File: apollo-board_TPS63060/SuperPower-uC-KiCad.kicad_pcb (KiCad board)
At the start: 4 copper layers, 45.1 x 45.1 mm, 113 parts, among them J1 JST_PH_S2B_thru, J10 Conn_01x13_Male, J11 Conn_01x04_Male, J3 Conn_01x02_Male, J4 DNP/JST_ZH_S2B_thru, J5 DNP/JST_XH_S2B_thru, J6 Conn_01x02_Male, Q1 DMN2019UTS, Q10 2N7002A, Q11 2N7002A, Q12 DMP2035UVT, Q13 DMP2035UVT, Q14 DMP2035UVT, Q15 DMN3023L, Q2 Si3421DV, Q3 DMN3023L, Q4 2N7002A, Q5 DMP2035UVT, Q6 BSS84-7-F, Q9 2N7002A, SW1 DNP/SKRKAEE020, U1 AP9101CK6-AYTRG1, U10 TPS63060, U2 USB-C, U3 IP4220CZ6, U4 LTC4162EUFD-LAD, U5 RV-3028-C7, U6 TPS70933DBV, U9 TPS63060

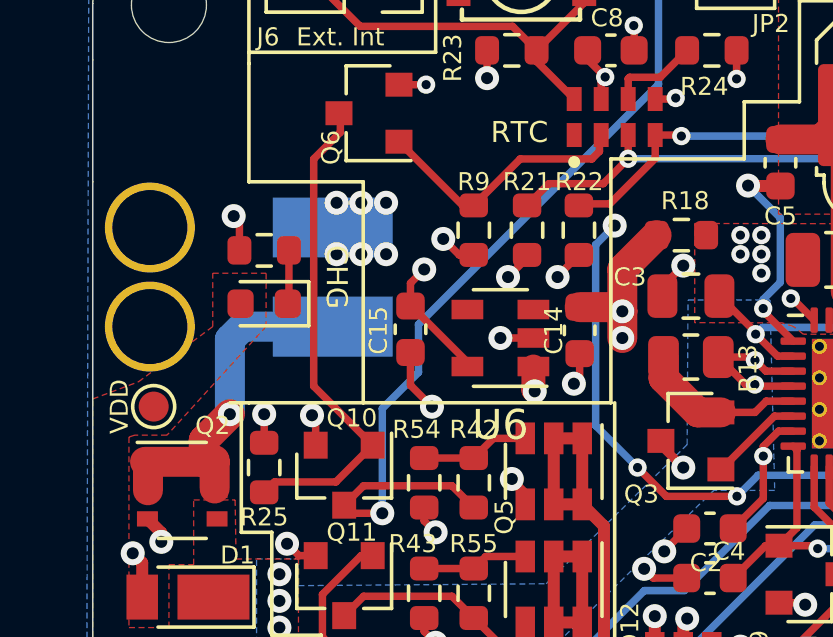
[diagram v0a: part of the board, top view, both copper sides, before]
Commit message: Update and clean "charger" sheet + add "Vcc" test point
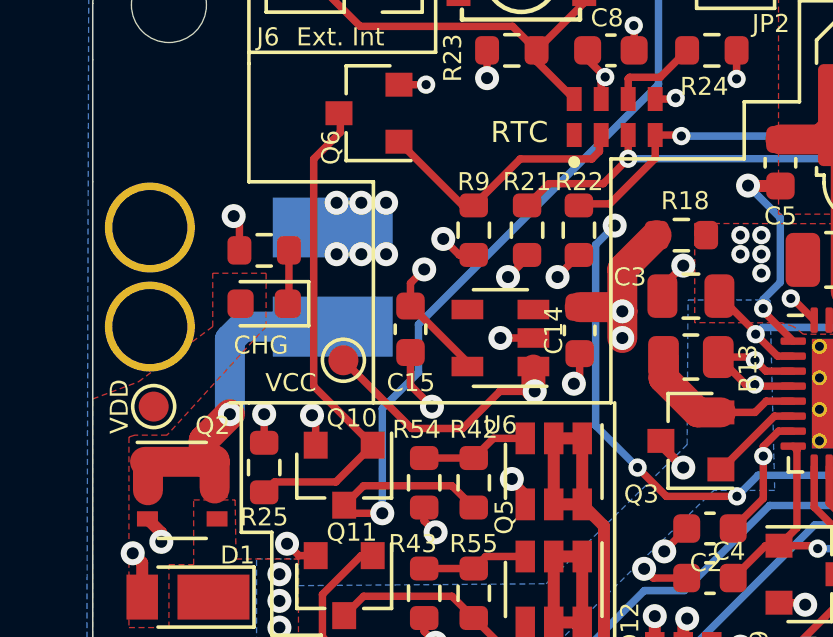
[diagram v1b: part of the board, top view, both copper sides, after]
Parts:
- added TP6: 3V3_I2C, TestPoint:TestPoint_Pad_D1.0mm, F.Cu at (126.3, 89.5)
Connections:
- C14 pad 1: /RTC/VIN -> VCC
- C7 pad 1: VCC -> VCCQ
- Q12 pad 1: /RTC/VIN -> VCC
- Q12 pad 2: /RTC/VIN -> VCC
- Q12 pad 4: VCC -> VCCQ
- Q12 pad 5: /RTC/VIN -> VCC
- Q12 pad 6: /RTC/VIN -> VCC
- Q14 pad 4: /RTC/VIN -> VCC
- Q15 pad 3: VCC -> VCCQ
- Q5 pad 4: /RTC/VIN -> VCC
- R13 pad 1: VCC -> VCCQ
- R17 pad 1: VCC -> VCCQ
- R18 pad 1: /RTC/VIN -> VCC
- R18 pad 2: VCC -> VCCQ
- R42 pad 2: /RTC/VIN -> VCC
- R43 pad 2: /RTC/VIN -> VCC
- U4 pad 27: VCC -> VCCQ
- U4 pad 28: VCC -> VCCQ
- U4 pad 3: VCC -> VCCQ
- U4 pad 4: VCC -> VCCQ
- U6 pad 1: /RTC/VIN -> VCC
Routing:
- net /RTC/VIN: track 14.6 -> 0.00 mm, vias 11 -> 0
- net VCC: track 10.1 -> 22.4 mm
- net VCCQ: track 0.00 -> 10.1 mm, vias 0 -> 11
- added copper zone on F.Cu, net VCCQ
- added copper zone on In2.Cu, net VCCQ
- removed copper zone on In2.Cu, net /RTC/VIN
- removed copper zone on F.Cu, net VCC
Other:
- board text added: "VCC"

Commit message: Rename some power signal on Schematic to improve readability.
+ Misc. updates
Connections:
- net /~SMBALERT renamed Net-(J10-Pad13)

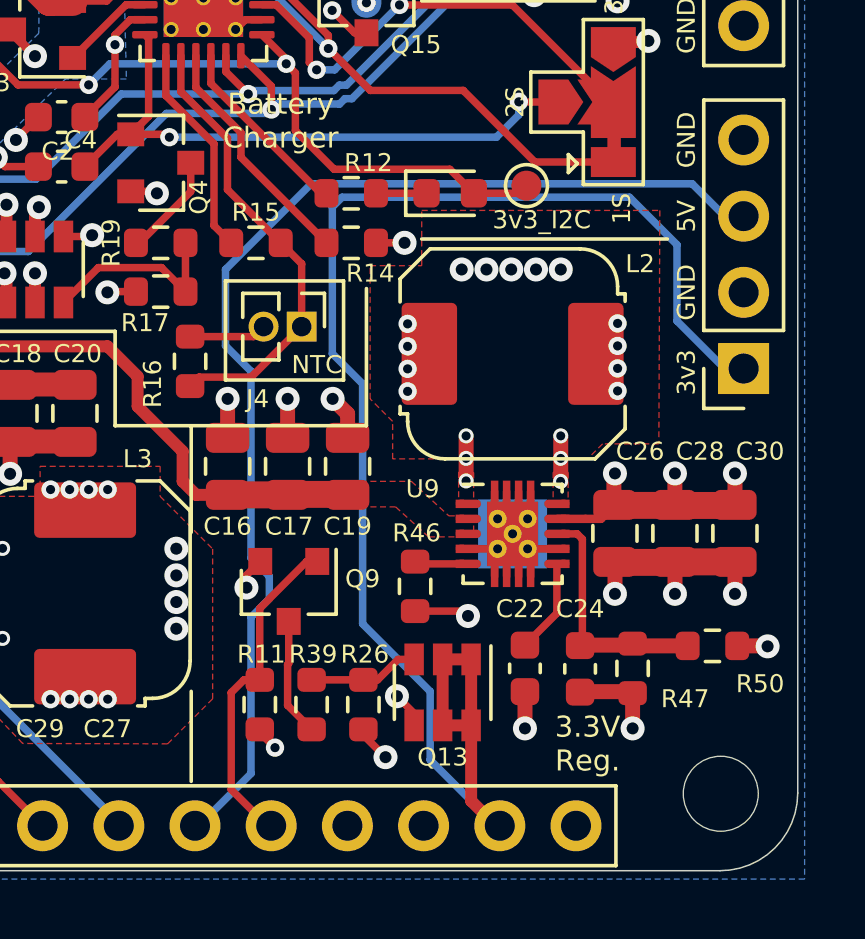
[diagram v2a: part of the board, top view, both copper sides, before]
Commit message: Improve Power tracks width on Bottom Layer
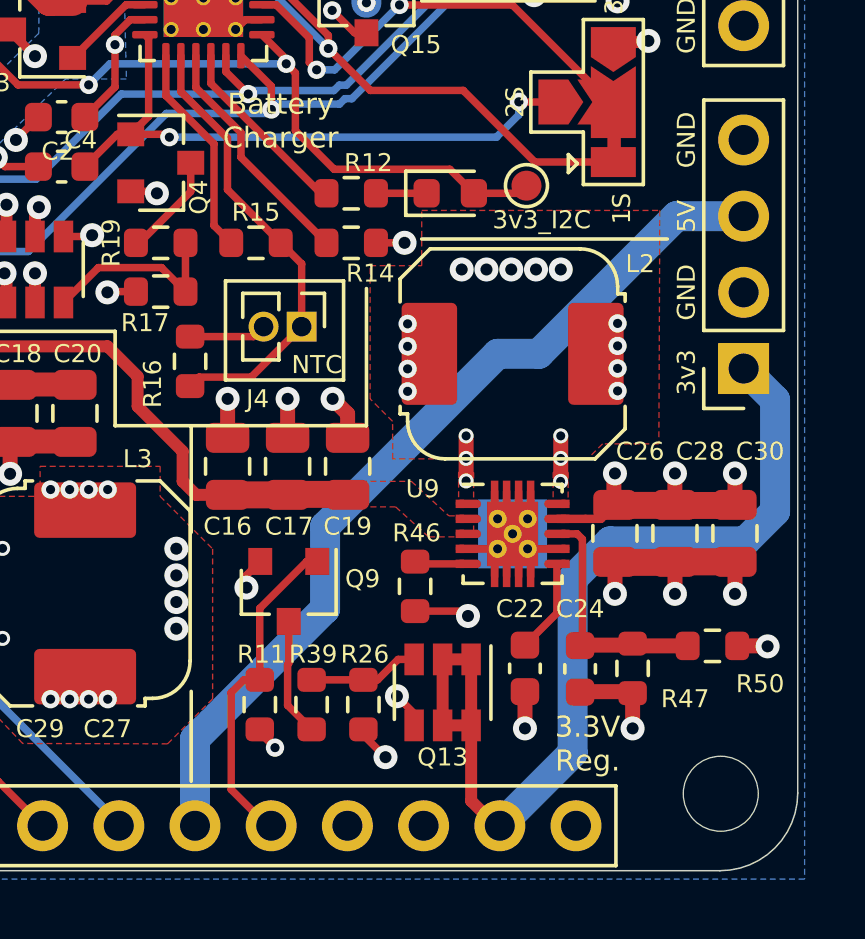
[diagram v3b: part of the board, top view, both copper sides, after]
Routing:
- net /3v3: track 50.3 -> 32.3 mm
- net /5V: track 61.7 -> 53.1 mm
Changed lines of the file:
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@@
     (thickness 1.6)
     (drawings 122)
-    (tracks 1000)
+    (tracks 992)
     (zones 0)
     (modules 114)
@@
     (1 In1.Cu power hide)
     (2 In2.Cu signal hide)
-    (31 B.Cu signal hide)
+    (31 B.Cu signal)
     (32 B.Adhes user)
     (33 F.Adhes user)
@@
   )
   (setup
-    (last_trace_width 0.25)
+    (last_trace_width 1)
     (user_trace_width 0.2)
     (user_trace_width 0.25)
@@
   (via (at 128.589 113.515) (size 0.8) (drill 0.4) (layers F.Cu B.Cu) (net 59))
   (via (at 130.589 114.265) (size 0.8) (drill 0.4) (layers F.Cu B.Cu) (net 59))
-  (segment (start 159.574989 97.344989) (end 160.655 98.425) (width 0.25) (layer B.Cu) (net 59))
-  (segment (start 146.876011 97.344989) (end 159.574989 97.344989) (width 0.25) (layer B.Cu) (net 59))
-  (segment (start 144.018 102.743) (end 144.018 100.203) (width 0.25) (layer B.Cu) (net 59))
-  (segment (start 144.870001 109.824499) (end 144.870001 103.595001) (width 0.25) (layer B.Cu) (net 59))
-  (segment (start 145.4785 111.182002) (end 145.4785 110.432998) (width 0.25) (layer B.Cu) (net 59))
-  (segment (start 144.870001 103.595001) (end 144.018 102.743) (width 0.25) (layer B.Cu) (net 59))
-  (segment (start 145.4785 110.432998) (end 144.870001 109.824499) (width 0.25) (layer B.Cu) (net 59))
-  (segment (start 144.870001 111.790501) (end 145.4785 111.182002) (width 0.25) (layer B.Cu) (net 59))
-  (segment (start 144.018 100.203) (end 146.876011 97.344989) (width 0.25) (layer B.Cu) (net 59))
-  (segment (start 144.870001 117.003999) (end 144.870001 111.790501) (width 0.25) (layer B.Cu) (net 59))
-  (segment (start 143.002 118.872) (end 144.870001 117.003999) (width 0.25) (layer B.Cu) (net 59))
   (segment (start 129.5 114.3) (end 131.5 114.3) (width 0.8) (layer F.Cu) (net 59))
   (segment (start 133.5 114.3) (end 131.5 114.3) (width 0.8) (layer F.Cu) (net 59))
@@
   (segment (start 133.839 113.961) (end 133.5 114.3) (width 0.25) (layer F.Cu) (net 59))
   (segment (start 133.839 112.475) (end 133.839 113.961) (width 0.28) (layer F.Cu) (net 59))
+  (segment (start 159.052799 98.425) (end 161.29 98.425) (width 1) (layer B.Cu) (net 59))
+  (segment (start 154.462799 103.015) (end 159.052799 98.425) (width 1) (layer B.Cu) (net 59))
+  (segment (start 153.089 103.015) (end 154.462799 103.015) (width 1) (layer B.Cu) (net 59))
+  (segment (start 147.339 108.765) (end 153.089 103.015) (width 1) (layer B.Cu) (net 59))
+  (segment (start 147.339 111.515) (end 147.339 108.765) (width 1) (layer B.Cu) (net 59))
+  (segment (start 143.002 115.852) (end 147.339 111.515) (width 1) (layer B.Cu) (net 59))
+  (segment (start 143.002 118.745) (end 143.002 115.852) (width 1) (layer B.Cu) (net 59))
   (segment (start 152.207 113.2) (end 151.257 113.2) (width 0.4) (layer F.Cu) (net 60))
   (segment (start 151.257 113.2) (end 151.257 115.4) (width 0.4) (layer F.Cu) (net 60))
@@
   (segment (start 152.207 117.917) (end 153.162 118.872) (width 0.4) (layer F.Cu) (net 60))
   (segment (start 152.207 115.4) (end 152.207 117.917) (width 0.4) (layer F.Cu) (net 60))
-  (segment (start 147.906599 97.794999) (end 157.484999 97.794999) (width 0.25) (layer B.Cu) (net 60))
-  (segment (start 157.484999 97.794999) (end 159.0675 99.3775) (width 0.25) (layer B.Cu) (net 60))
-  (segment (start 147.578999 98.122599) (end 147.906599 97.794999) (width 0.25) (layer B.Cu) (net 60))
-  (segment (start 147.578999 103.004999) (end 147.578999 98.122599) (width 0.25) (layer B.Cu) (net 60))
-  (segment (start 148.589 104.015) (end 147.578999 103.004999) (width 0.25) (layer B.Cu) (net 60))
-  (segment (start 148.589 112.015) (end 148.589 104.015) (width 0.25) (layer B.Cu) (net 60))
-  (segment (start 150.839 114.265) (end 148.589 112.015) (width 0.25) (layer B.Cu) (net 60))
-  (segment (start 159.0675 101.9175) (end 160.655 103.505) (width 0.25) (layer B.Cu) (net 60))
-  (segment (start 150.839 116.549) (end 150.839 114.265) (width 0.25) (layer B.Cu) (net 60))
-  (segment (start 159.0675 99.3775) (end 159.0675 101.9175) (width 0.25) (layer B.Cu) (net 60))
-  (segment (start 153.162 118.872) (end 150.839 116.549) (width 0.25) (layer B.Cu) (net 60))
+  (segment (start 162.339 104.554) (end 161.29 103.505) (width 1) (layer B.Cu) (net 60))
+  (segment (start 161.339 109.265) (end 162.339 108.265) (width 1) (layer B.Cu) (net 60))
+  (segment (start 156.839 109.265) (end 161.339 109.265) (width 1) (layer B.Cu) (net 60))
+  (segment (start 162.339 108.265) (end 162.339 104.554) (width 1) (layer B.Cu) (net 60))
+  (segment (start 155.589 110.515) (end 156.839 109.265) (width 1) (layer B.Cu) (net 60))
+  (segment (start 155.589 116.318) (end 155.589 110.515) (width 1) (layer B.Cu) (net 60))
+  (segment (start 153.162 118.745) (end 155.589 116.318) (width 1) (layer B.Cu) (net 60))
   (via (at 162.089 112.765) (size 0.8) (drill 0.4) (layers F.Cu B.Cu) (net 61))
   (via (at 149.352 116.459) (size 0.8) (drill 0.4) (layers F.Cu B.Cu) (net 61))

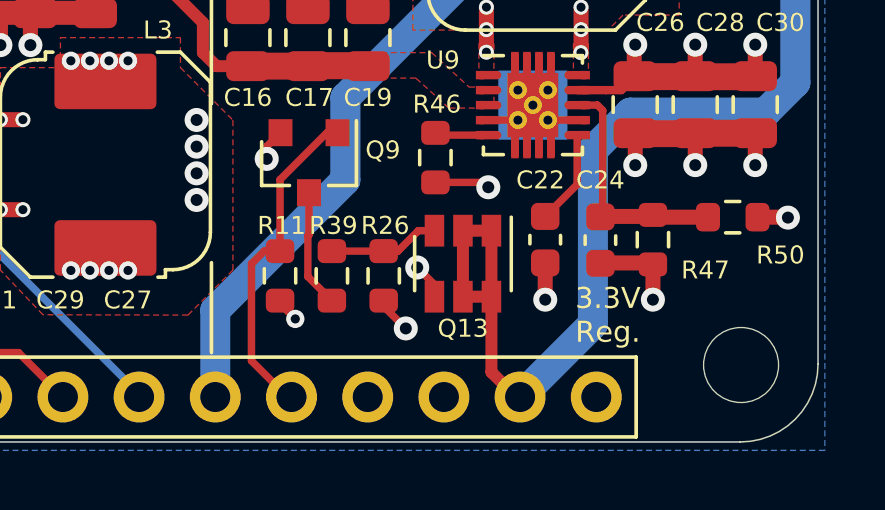
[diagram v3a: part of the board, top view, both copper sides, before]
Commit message: Improve Power Tracks width and Vias on Top Layer (+3.3V regulator)
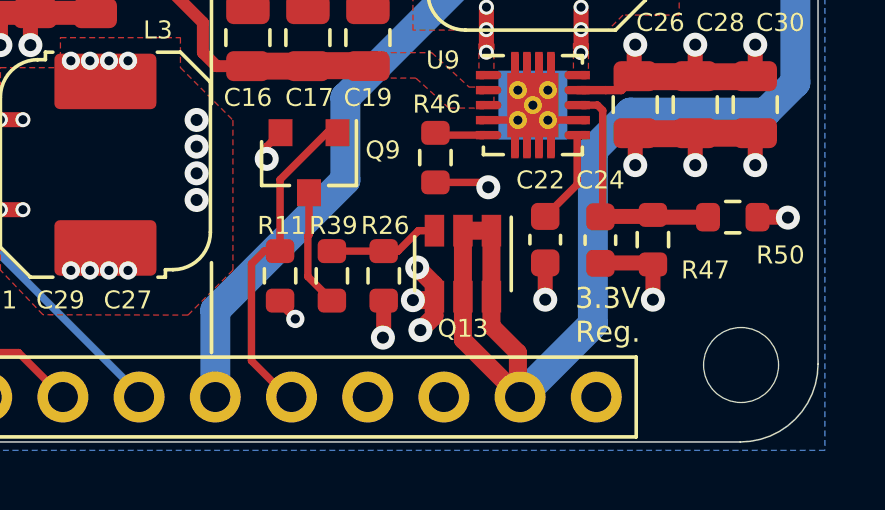
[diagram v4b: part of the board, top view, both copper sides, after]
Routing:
- net /3v3: track 32.3 -> 35.5 mm
- net /3v3_MCU: track 14.5 -> 16.6 mm, vias 7 -> 9
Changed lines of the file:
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@@
     (thickness 1.6)
     (drawings 122)
-    (tracks 992)
+    (tracks 1001)
     (zones 0)
     (modules 114)
@@
     (0 F.Cu signal)
     (1 In1.Cu power hide)
-    (2 In2.Cu signal hide)
-    (31 B.Cu signal)
+    (2 In2.Cu signal)
+    (31 B.Cu signal hide)
     (32 B.Adhes user)
     (33 F.Adhes user)
@@
   )
   (setup
-    (last_trace_width 1)
+    (last_trace_width 0.5)
     (user_trace_width 0.2)
     (user_trace_width 0.25)
@@
     (user_trace_width 0.4)
     (user_trace_width 0.5)
+    (user_trace_width 0.6)
     (user_trace_width 0.8)
     (user_trace_width 1)
@@
   (segment (start 143.002 115.852) (end 147.339 111.515) (width 1) (layer B.Cu) (net 59))
   (segment (start 143.002 118.745) (end 143.002 115.852) (width 1) (layer B.Cu) (net 59))
-  (segment (start 152.207 113.2) (end 151.257 113.2) (width 0.4) (layer F.Cu) (net 60))
-  (segment (start 151.257 113.2) (end 151.257 115.4) (width 0.4) (layer F.Cu) (net 60))
-  (segment (start 151.257 115.4) (end 152.207 115.4) (width 0.4) (layer F.Cu) (net 60))
-  (segment (start 152.207 113.2) (end 152.207 115.4) (width 0.4) (layer F.Cu) (net 60))
-  (segment (start 152.207 117.917) (end 153.162 118.872) (width 0.4) (layer F.Cu) (net 60))
-  (segment (start 152.207 115.4) (end 152.207 117.917) (width 0.4) (layer F.Cu) (net 60))
+  (segment (start 152.207 113.2) (end 151.257 113.2) (width 0.6) (layer F.Cu) (net 60))
+  (segment (start 151.257 113.2) (end 151.257 115.4) (width 0.6) (layer F.Cu) (net 60))
+  (segment (start 152.207 113.2) (end 152.207 115.4) (width 0.6) (layer F.Cu) (net 60))
   (segment (start 162.339 104.554) (end 161.29 103.505) (width 1) (layer B.Cu) (net 60))
   (segment (start 161.339 109.265) (end 162.339 108.265) (width 1) (layer B.Cu) (net 60))
@@
   (segment (start 155.589 116.318) (end 155.589 110.515) (width 1) (layer B.Cu) (net 60))
   (segment (start 153.162 118.745) (end 155.589 116.318) (width 1) (layer B.Cu) (net 60))
+  (segment (start 153.089 118.799) (end 153.162 118.872) (width 0.5) (layer F.Cu) (net 60))
+  (segment (start 153.089 117.265) (end 153.089 118.799) (width 0.6) (layer F.Cu) (net 60))
+  (segment (start 152.207 116.383) (end 153.089 117.265) (width 0.6) (layer F.Cu) (net 60))
+  (segment (start 152.207 115.4) (end 152.207 116.383) (width 0.6) (layer F.Cu) (net 60))
+  (segment (start 151.257 116.84) (end 153.162 118.745) (width 0.6) (layer F.Cu) (net 60))
+  (segment (start 151.257 115.4) (end 151.257 116.84) (width 0.6) (layer F.Cu) (net 60))
   (via (at 162.089 112.765) (size 0.8) (drill 0.4) (layers F.Cu B.Cu) (net 61))
-  (via (at 149.352 116.459) (size 0.8) (drill 0.4) (layers F.Cu B.Cu) (net 61))
-  (segment (start 148.6154 115.7224) (end 149.352 116.459) (width 0.25) (layer F.Cu) (net 61))
-  (segment (start 148.6154 115.5314) (end 148.6154 115.7224) (width 0.25) (layer F.Cu) (net 61))
   (via (at 149.733 114.427) (size 0.8) (drill 0.4) (layers F.Cu B.Cu) (net 61))
-  (segment (start 150.307 115.001) (end 149.733 114.427) (width 0.25) (layer F.Cu) (net 61))
-  (segment (start 150.307 115.4) (end 150.307 115.001) (width 0.25) (layer F.Cu) (net 61))
+  (segment (start 150.307 115.4) (end 150.307 115.001) (width 0.6) (layer F.Cu) (net 61))
+  (segment (start 150.307 115.001) (end 149.733 114.427) (width 0.6) (layer F.Cu) (net 61))
   (via (at 157 107) (size 0.8) (drill 0.4) (layers F.Cu B.Cu) (net 61))
   (segment (start 156.9658 108.0664) (end 156.9658 107.1103) (width 0.5) (layer F.Cu) (net 61))
@@
   (segment (start 151.914 111.59) (end 152.076347 111.752347) (width 0.25) (layer F.Cu) (net 61))
   (segment (start 150.339 111.59) (end 151.914 111.59) (width 0.25) (layer F.Cu) (net 61))
+  (via (at 149.589 115.515) (size 0.8) (drill 0.4) (layers F.Cu B.Cu) (net 61))
+  (via (at 149.839007 116.514993) (size 0.8) (drill 0.4) (layers F.Cu B.Cu) (net 61))
+  (segment (start 150.307 115.4) (end 150.307 116.047) (width 0.6) (layer F.Cu) (net 61))
+  (segment (start 150.307 116.047) (end 149.839007 116.514993) (width 0.6) (layer F.Cu) (net 61))
+  (segment (start 150.192 115.515) (end 150.307 115.4) (width 0.5) (layer F.Cu) (net 61))
+  (segment (start 149.589 115.515) (end 150.192 115.515) (width 0.6) (layer F.Cu) (net 61))
+  (segment (start 148.6154 116.7386) (end 148.589 116.765) (width 0.5) (layer F.Cu) (net 61))
+  (segment (start 148.6154 115.5314) (end 148.6154 116.7386) (width 0.5) (layer F.Cu) (net 61))
+  (via (at 148.589 116.765) (size 0.8) (drill 0.4) (layers F.Cu B.Cu) (net 61))
   (segment (start 138.93289 93.152) (end 138.922 93.152) (width 0.25) (layer F.Cu) (net 62))
   (segment (start 140.70769 91.3772) (end 138.93289 93.152) (width 0.25) (layer F.Cu) (net 62))
@@
     (polygon
       (pts
-        (xy 162.306 116.713) (xy 149.86 116.713) (xy 149.86 120.269) (xy 146.431 120.269) (xy 146.431 110.2995)
-        (xy 149.5425 110.2995) (xy 156.339 110.28225) (xy 156.339 107.015) (xy 157.089 106.265) (xy 162.306 106.265)
+        (xy 162.306 116.713) (xy 150.839 116.765) (xy 149.86 117.515) (xy 149.86 120.269) (xy 146.431 120.269)
+        (xy 146.431 110.2995) (xy 149.5425 110.2995) (xy 156.339 110.28225) (xy 156.339 107.015) (xy 157.089 106.265)
+        (xy 162.306 106.265)
       )
     )

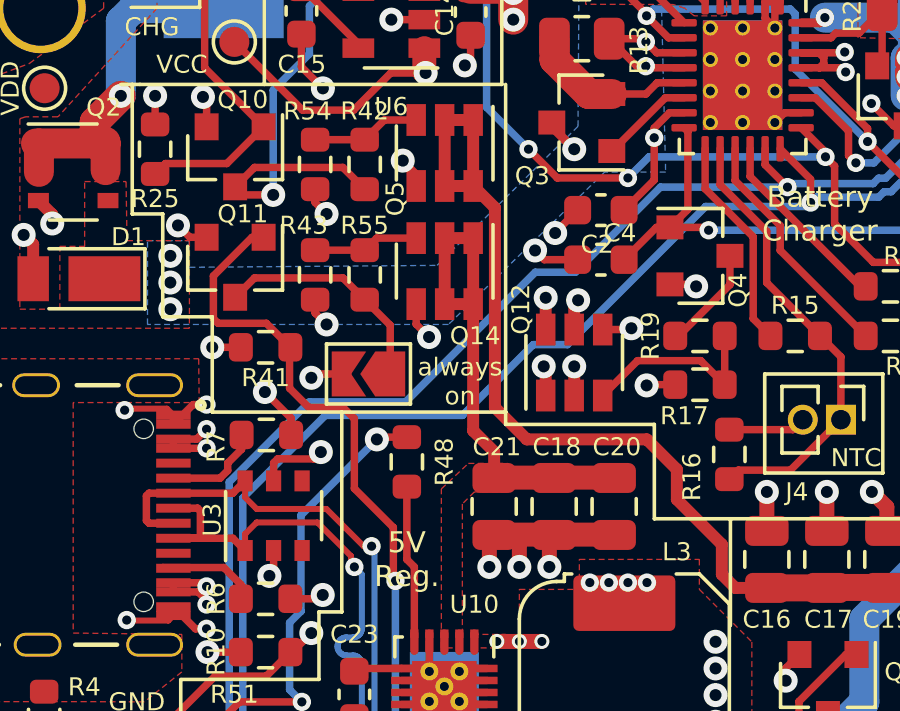
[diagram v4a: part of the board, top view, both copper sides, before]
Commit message: Improve PowerTracks width and Vias on Top Layer (+5.0V)
+ Flip JP3
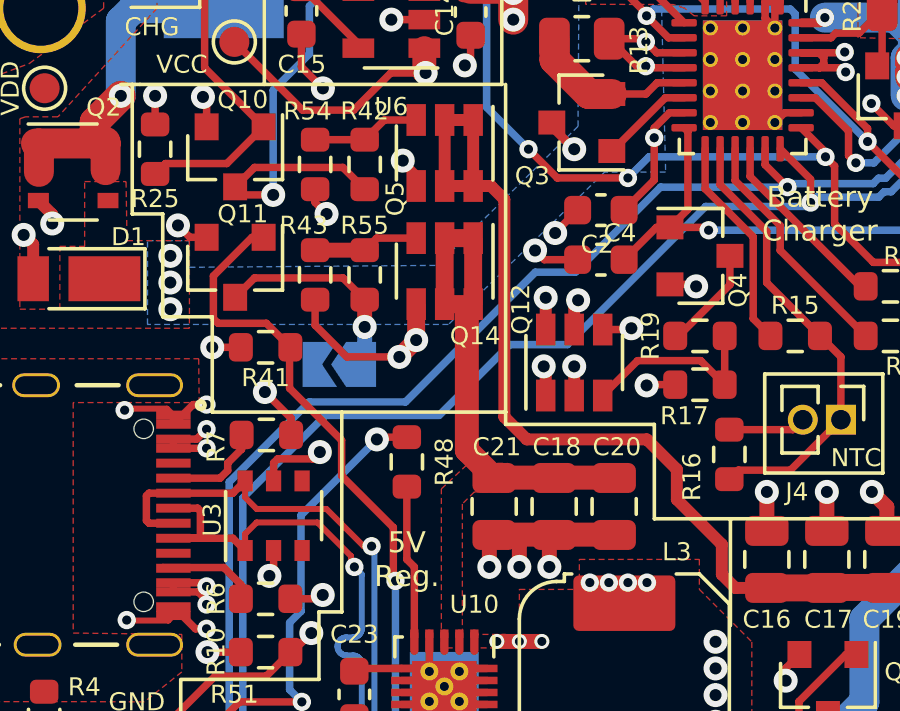
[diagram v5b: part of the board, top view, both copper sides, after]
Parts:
- JP3: moved to B.Cu
- moved JP3 1.02 mm to (129.8, 100.3)
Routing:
- net VCC: track 22.4 -> 26.2 mm
- net GND: track 110.7 -> 109.5 mm, vias 74 -> 73
- net /EN_5V: track 32.9 -> 32.3 mm
- net Net-(JP3-Pad1): track 7.72 -> 7.25 mm, vias 0 -> 1
